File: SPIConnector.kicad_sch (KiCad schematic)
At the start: 14 parts, among them J15 SPI

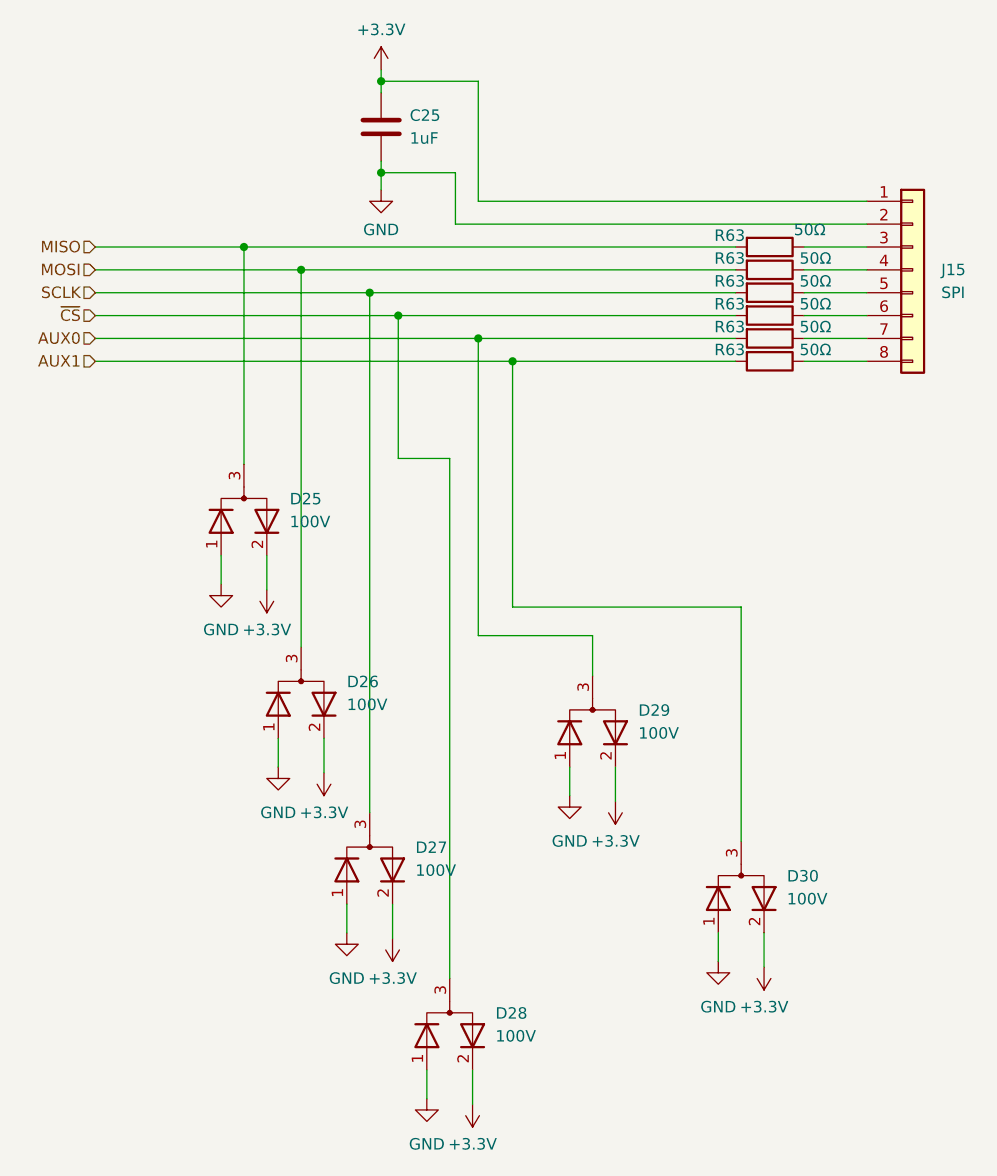
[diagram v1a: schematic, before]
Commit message: Finished schematic. Move to PCB.
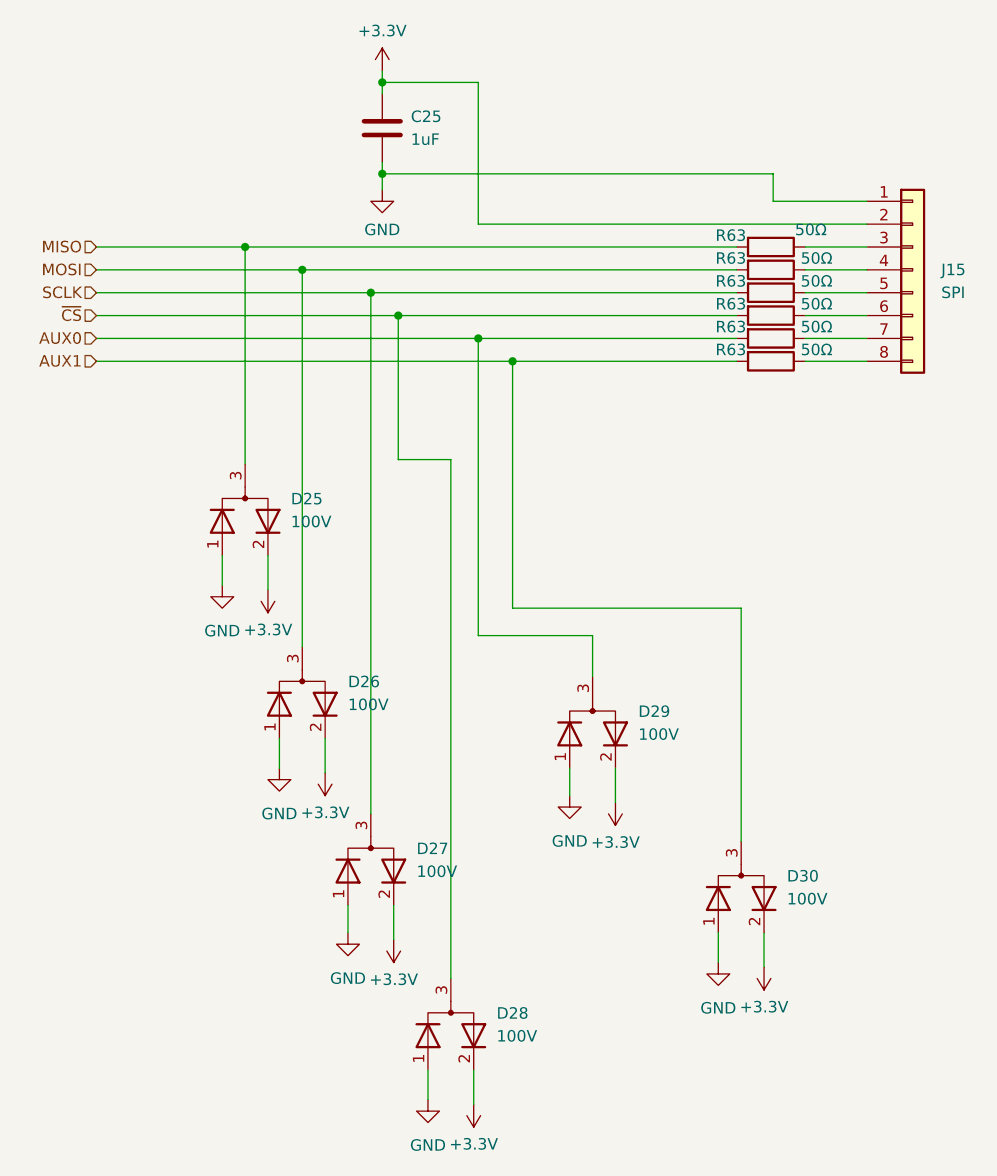
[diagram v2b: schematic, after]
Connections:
- net +3.3V: now also J15.2 (Pin_2); no longer J15.1 (Pin_1)
- net GND: now also J15.1 (Pin_1); no longer J15.2 (Pin_2)
